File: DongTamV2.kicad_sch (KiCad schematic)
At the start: 9 parts, among them J1 KF128, J11 KF128, J12 KF128, J13 KF128, J2 KF128

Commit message: finish some unconnect pins, draw edge cut board
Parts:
- added H1, H2, H3, H4: MountingHole, MountingHole:MountingHole_3.2mm_M3, symbol SpiritBoi_Library:MountingHole
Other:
- sheet PCF8563 ports: added i2c{I2C}; removed none

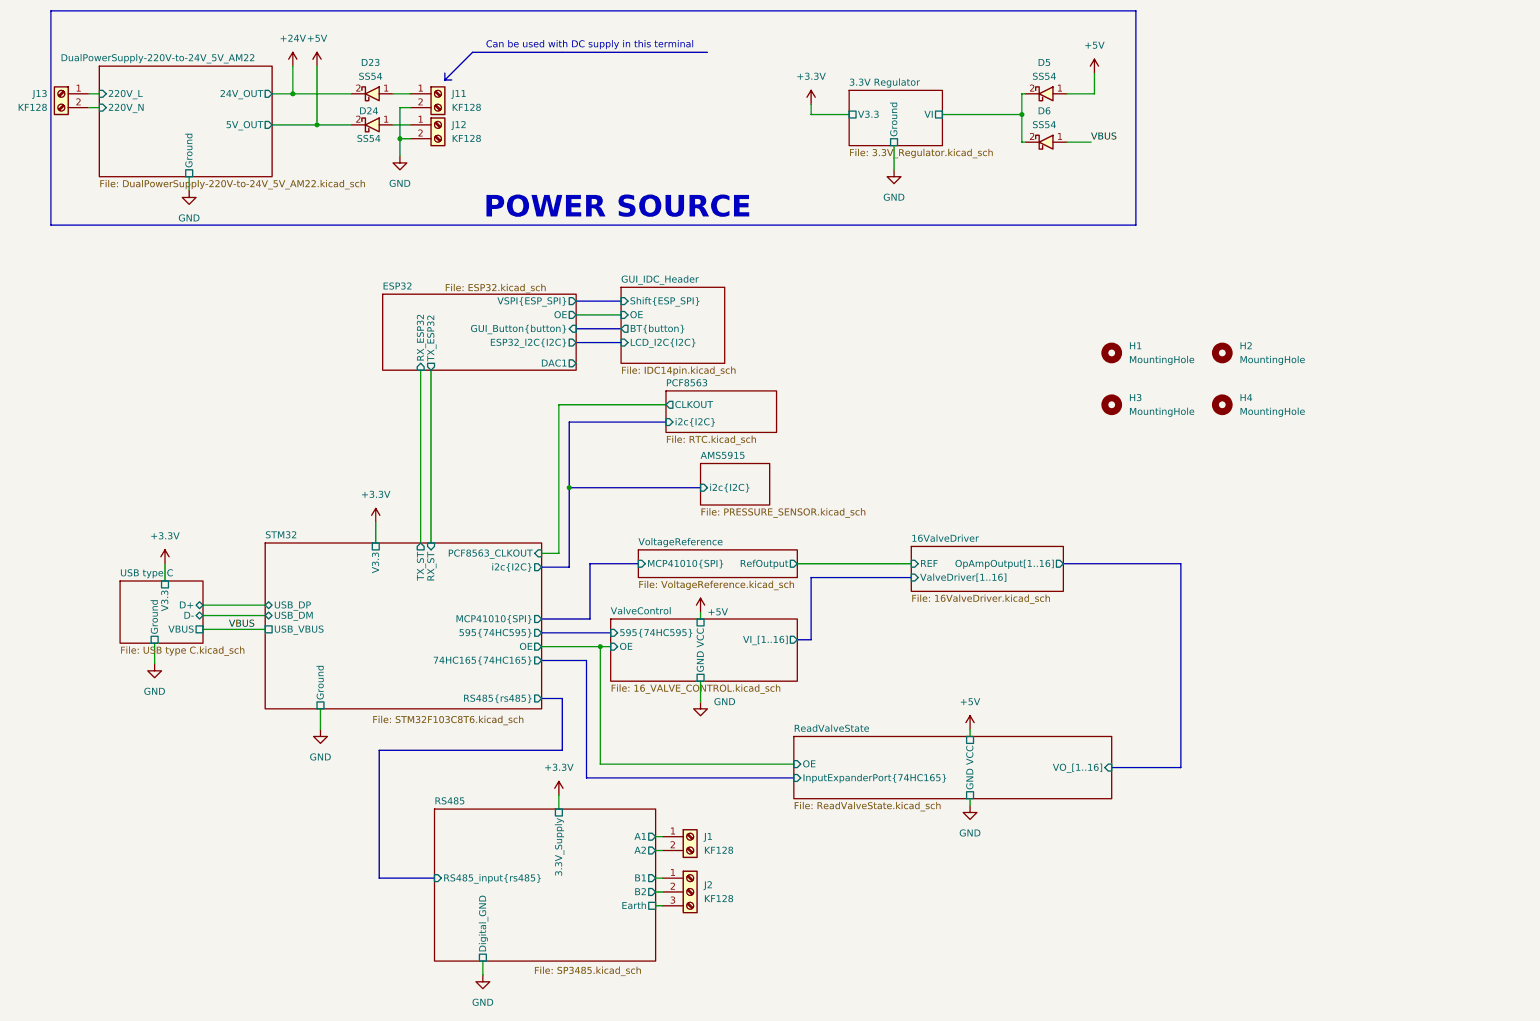
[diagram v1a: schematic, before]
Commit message: Add LORA, SDcard and Volt to 4_20mA scheamtic
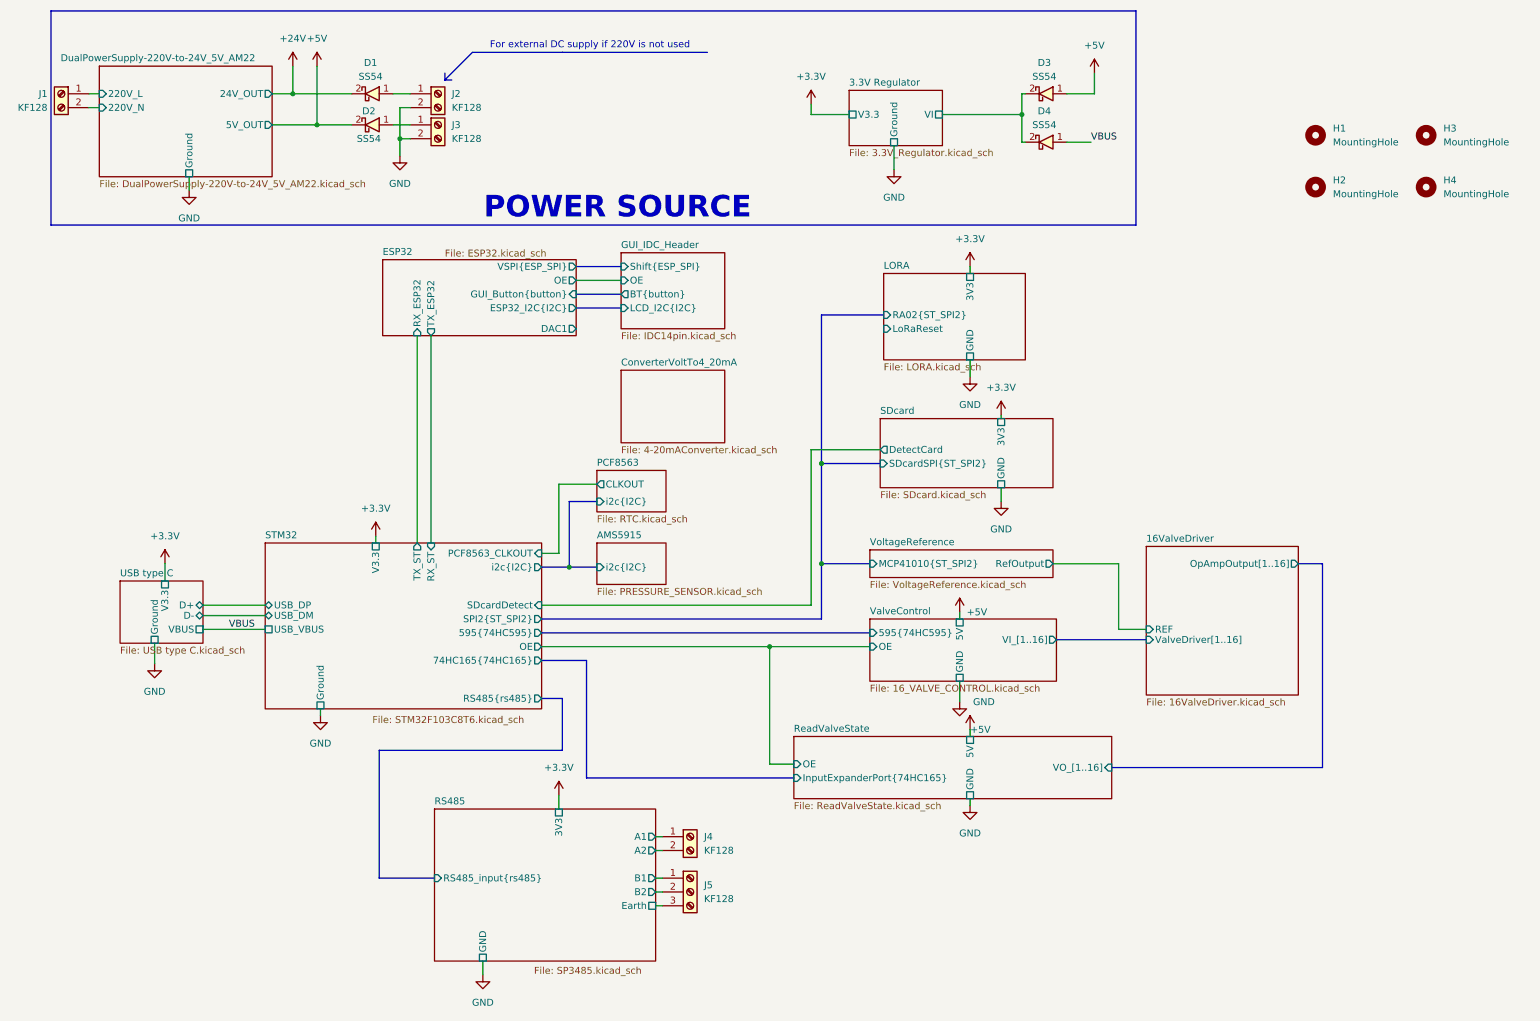
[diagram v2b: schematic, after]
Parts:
- renumbered D23 to D1, D24 to D2, D5 to D3, D6 to D4, H3 to H2, H2 to H3, J13 to J1, J11 to J2, J12 to J3, J1 to J4, J2 to J5
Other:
- added sheet ConverterVoltTo4_20mA (4-20mAConverter.kicad_sch)
- added sheet LORA (LORA.kicad_sch)
- added sheet SDcard (SDcard.kicad_sch)
- sheet RS485 ports: added 3V3, GND; removed 3.3V_Supply, Digital_GND
- sheet ReadValveState ports: added 5V; removed VCC
- sheet STM32 ports: added SDcardDetect, SPI2{ST_SPI2}; removed MCP41010{SPI}
- sheet ValveControl ports: added 5V; removed VCC
- sheet VoltageReference ports: added MCP41010{ST_SPI2}; removed MCP41010{SPI}
- note added: "For external DC supply if 220V is not used"
- note removed: "Can be used with DC supply in this terminal"
- moved on the sheet: H1, H2, H3, H4

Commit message: Add README, Lora received interrupt pin
Change LED pin from PB0 to PC13, PCF8563_CLKOUT to PC14
PB0 add Lora received interrupt pin
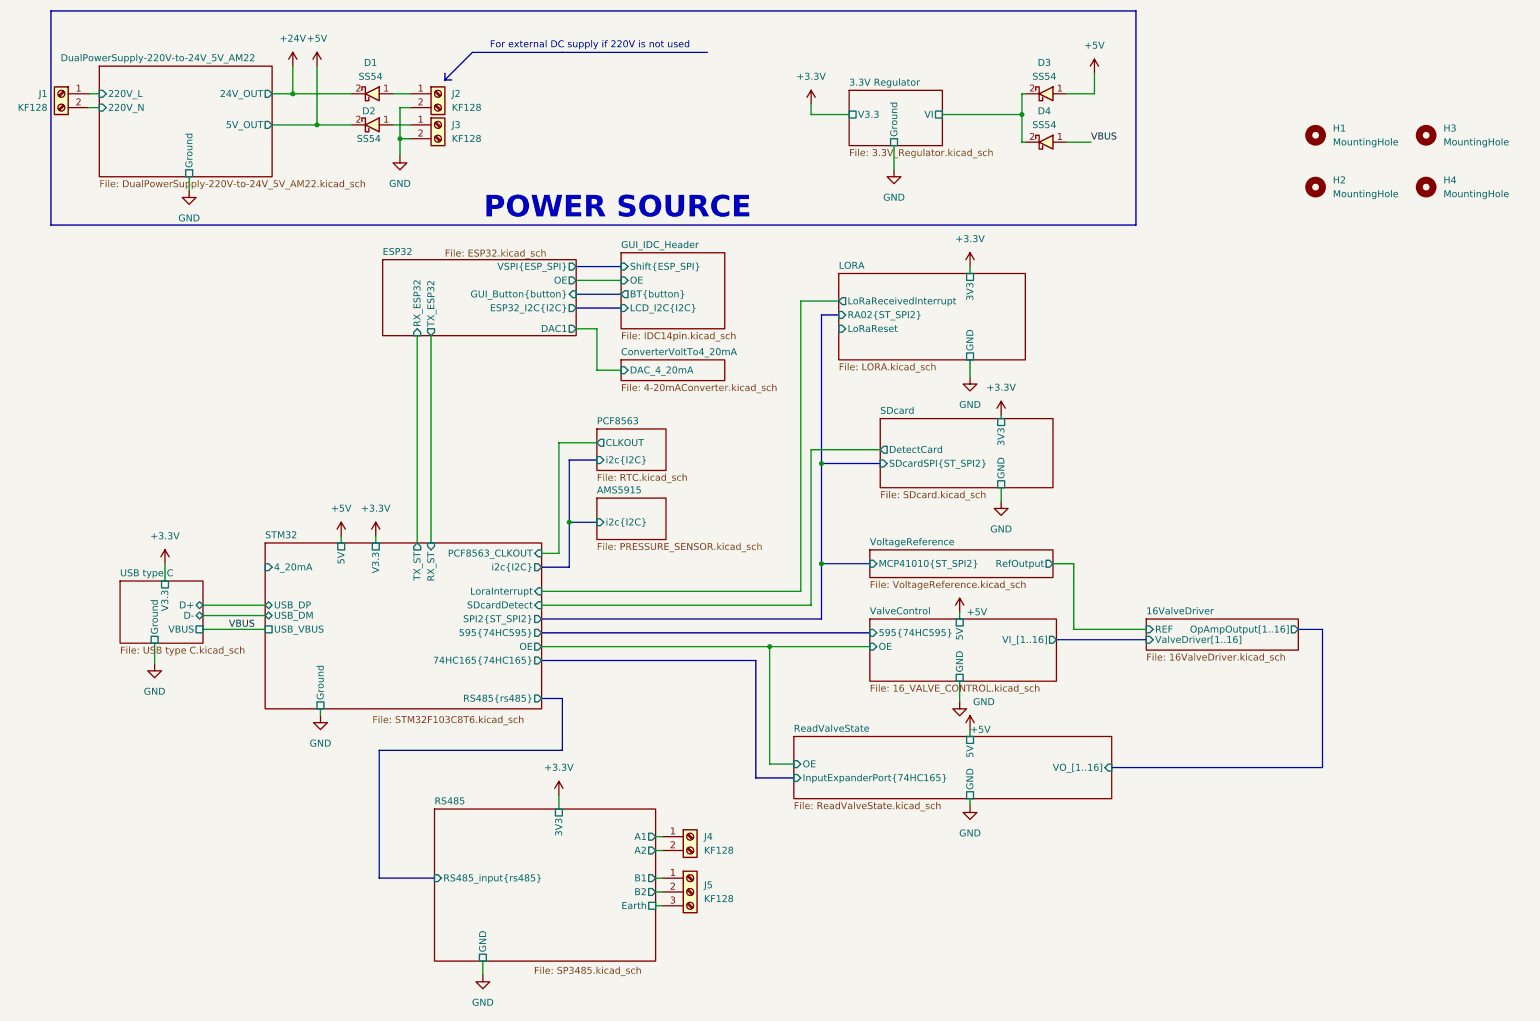
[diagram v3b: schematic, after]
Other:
- sheet ConverterVoltTo4_20mA ports: added DAC_4_20mA; removed none
- sheet LORA ports: added LoRaReceivedInterrupt; removed none
- sheet STM32 ports: added 4_20mA, 5V, LoraInterrupt; removed none

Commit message: Feat: Components's layout
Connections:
- net DualPowerSupply-220V-to-24V_5V_AM22/220V_L: now also J1.2 (Pin_2); no longer J1.1 (Pin_1)
- net DualPowerSupply-220V-to-24V_5V_AM22/220V_N: now also J1.1 (Pin_1); no longer J1.2 (Pin_2)
- net RS485/B1: now also J5.2 (Pin_2); no longer J5.1 (Pin_1)
- net RS485/B2: now also J5.3 (Pin_3); no longer J5.2 (Pin_2)
- net RS485/Earth: now also J5.1 (Pin_1); no longer J5.3 (Pin_3)
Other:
- moved on the sheet: J5
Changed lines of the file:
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@@
 	(wire
 		(pts
+			(xy 125.095 169.545) (xy 126.365 169.545)
+		)
+		(stroke
+			(width 0)
+			(type default)
+		)
+	)
+	(wire
+		(pts
 			(xy 104.14 129.54) (xy 146.05 129.54)
 		)
@@
 	(wire
 		(pts
+			(xy 20.955 30.48) (xy 22.86 30.48)
+		)
+		(stroke
+			(width 0)
+			(type default)
+		)
+	)
+	(wire
+		(pts
 			(xy 200.66 27.94) (xy 205.74 27.94)
 		)
@@
 	(wire
 		(pts
+			(xy 125.095 174.625) (xy 126.365 174.625)
+		)
+		(stroke
+			(width 0)
+			(type default)
+		)
+	)
+	(wire
+		(pts
 			(xy 114.3 92.075) (xy 107.315 92.075)
 		)
@@
 	(wire
 		(pts
-			(xy 125.095 174.625) (xy 126.365 174.625)
-		)
-		(stroke
-			(width 0)
-			(type default)
-		)
-	)
-	(wire
-		(pts
 			(xy 41.91 126.365) (xy 53.34 126.365)
 		)
@@
 		)
 	)
-	(wire
+	(bus
 		(pts
-			(xy 20.955 30.48) (xy 22.86 30.48)
+			(xy 155.575 95.885) (xy 166.37 95.885)
 		)
 		(stroke
@@
 		)
 	)
-	(bus
+	(wire
 		(pts
-			(xy 155.575 95.885) (xy 166.37 95.885)
+			(xy 63.5 140.97) (xy 63.5 142.24)
 		)
 		(stroke
@@
 	(wire
 		(pts
-			(xy 63.5 140.97) (xy 63.5 142.24)
+			(xy 125.095 172.085) (xy 126.365 172.085)
 		)
 		(stroke
@@
 	(wire
 		(pts
-			(xy 125.095 172.085) (xy 126.365 172.085)
-		)
-		(stroke
-			(width 0)
-			(type default)
-		)
-	)
-	(wire
-		(pts
 			(xy 182.88 157.48) (xy 182.88 158.75)
 		)
@@
 	(wire
 		(pts
-			(xy 125.095 177.165) (xy 126.365 177.165)
-		)
-		(stroke
-			(width 0)
-			(type default)
-		)
-	)
-	(wire
-		(pts
 			(xy 182.88 144.78) (xy 182.88 146.05)
 		)
@@
 	(symbol
 		(lib_id "SpiritBoi_Library:Screw_Terminal_01x03")
-		(at 131.445 174.625 0)
+		(at 131.445 172.085 0)
 		(unit 1)
 		(exclude_from_sim no)
@@
 		(fields_autoplaced yes)
 		(property "Reference" "J5"
-			(at 133.985 173.3549 0)
+			(at 133.985 170.8149 0)
 			(effects
 				(font
@@
 		)
 		(property "Value" "KF128"
-			(at 133.985 175.8949 0)
+			(at 133.985 173.3549 0)
 			(effects
 				(font
@@
 		)
 		(property "Footprint" "SpiritBoi_Footprint_Library:TerminalBlock_bornier-3_P5.08mm"
-			(at 131.445 174.625 0)
+			(at 131.445 172.085 0)
 			(effects
 				(font
@@
 		)
 		(property "Datasheet" "~"
-			(at 131.445 174.625 0)
+			(at 131.445 172.085 0)
 			(effects
 				(font
@@
 		)
 		(property "Description" "Generic screw terminal, single row, 01x03, script generated (kicad-library-utils/schlib/autogen/connector/)"
-			(at 131.445 174.625 0)
+			(at 131.445 172.085 0)
 			(effects
 				(font
@@
 		)
 		(pin "220V_L" input
-			(at 22.86 27.94 180)
+			(at 22.86 30.48 180)
 			(effects
 				(font
@@
 		)
 		(pin "220V_N" input
-			(at 22.86 30.48 180)
+			(at 22.86 27.94 180)
 			(effects
 				(font
@@
 		)
 		(pin "Earth" passive
-			(at 125.095 177.165 0)
+			(at 125.095 169.545 0)
 			(effects
 				(font
